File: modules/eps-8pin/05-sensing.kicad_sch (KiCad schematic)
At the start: 16 parts, among them U10 INA238, U11 INA238, U20 INA181A2IDBVR, U21 INA181A2IDBVR, U30 TLV7011DBVR, U31 TLV7011DBVR

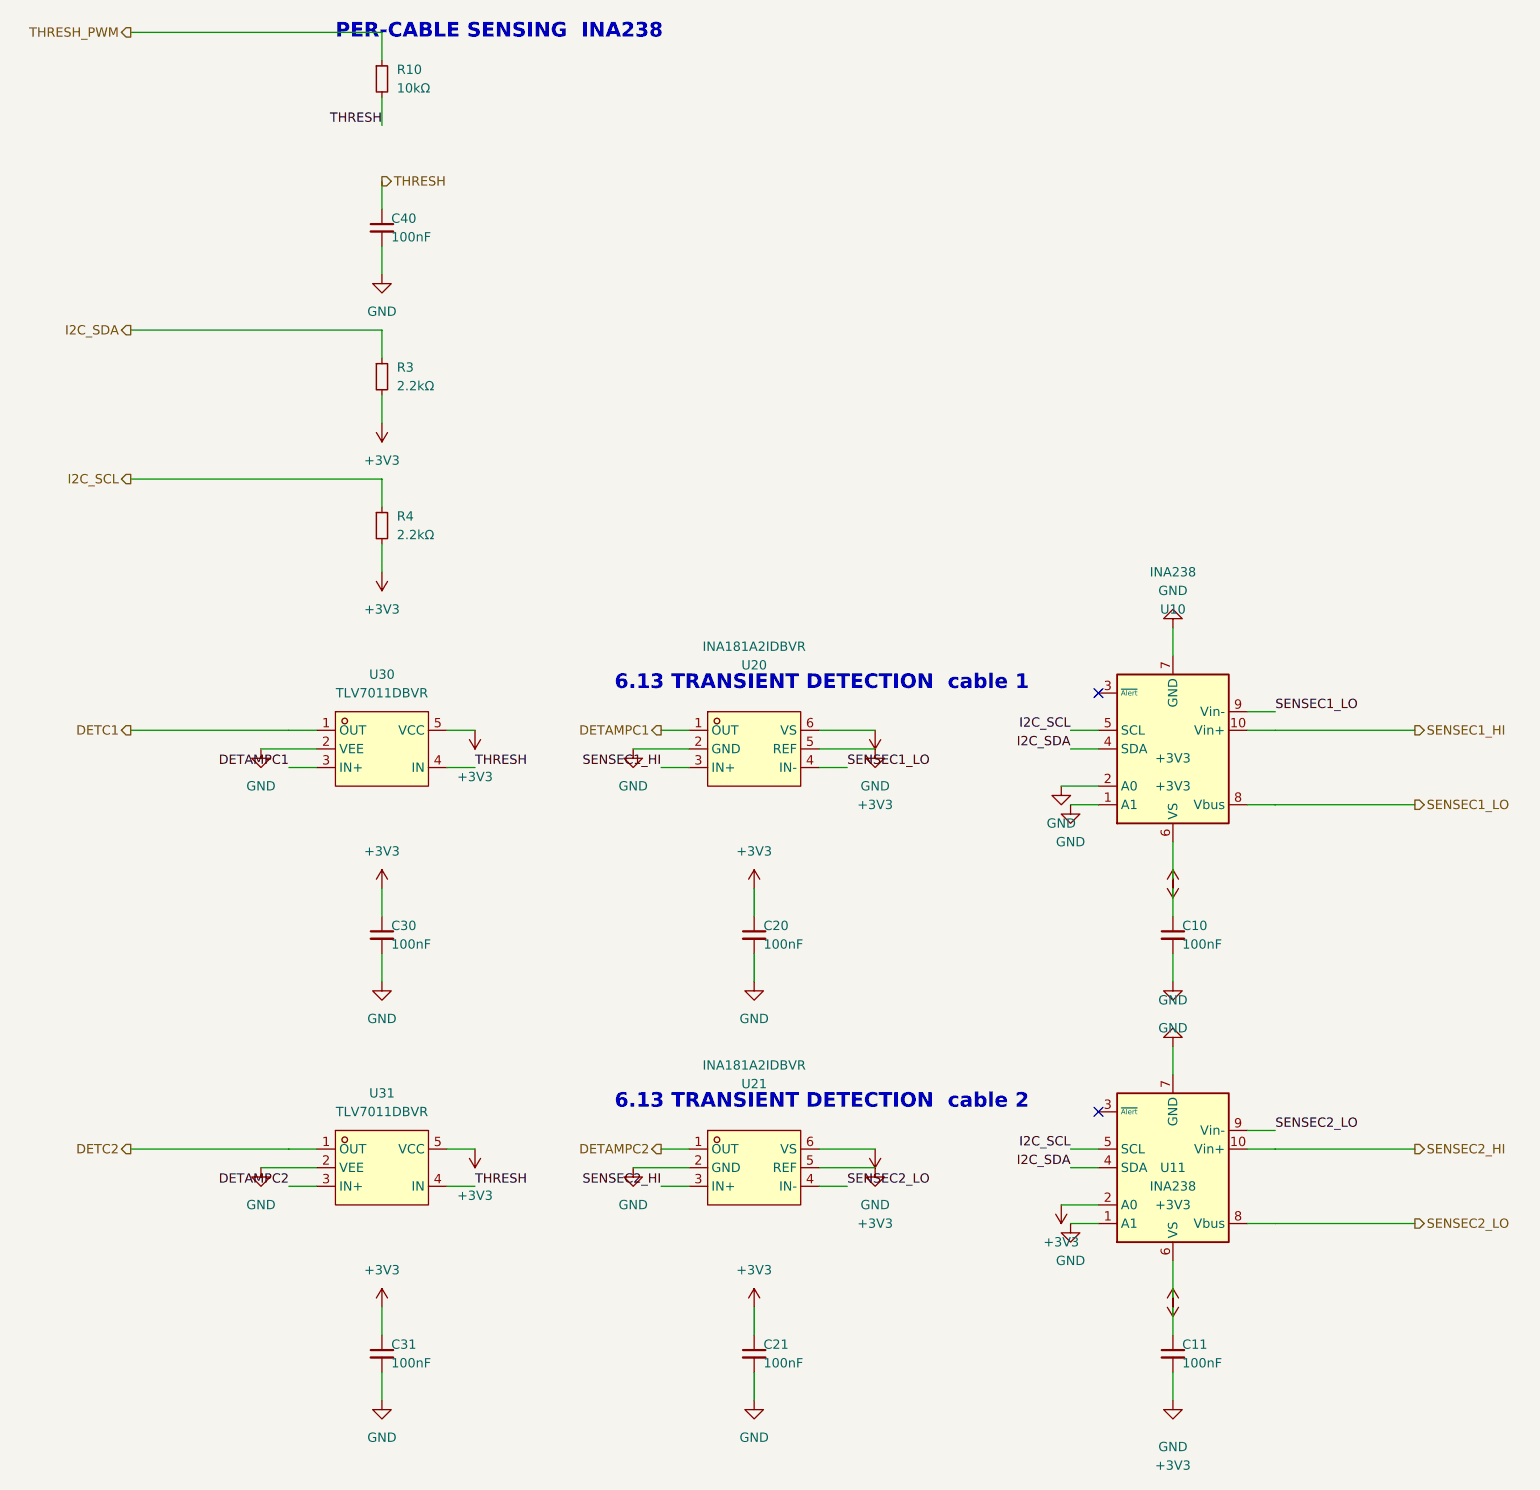
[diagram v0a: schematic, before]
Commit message: Looking through boards and figuring out outlines.
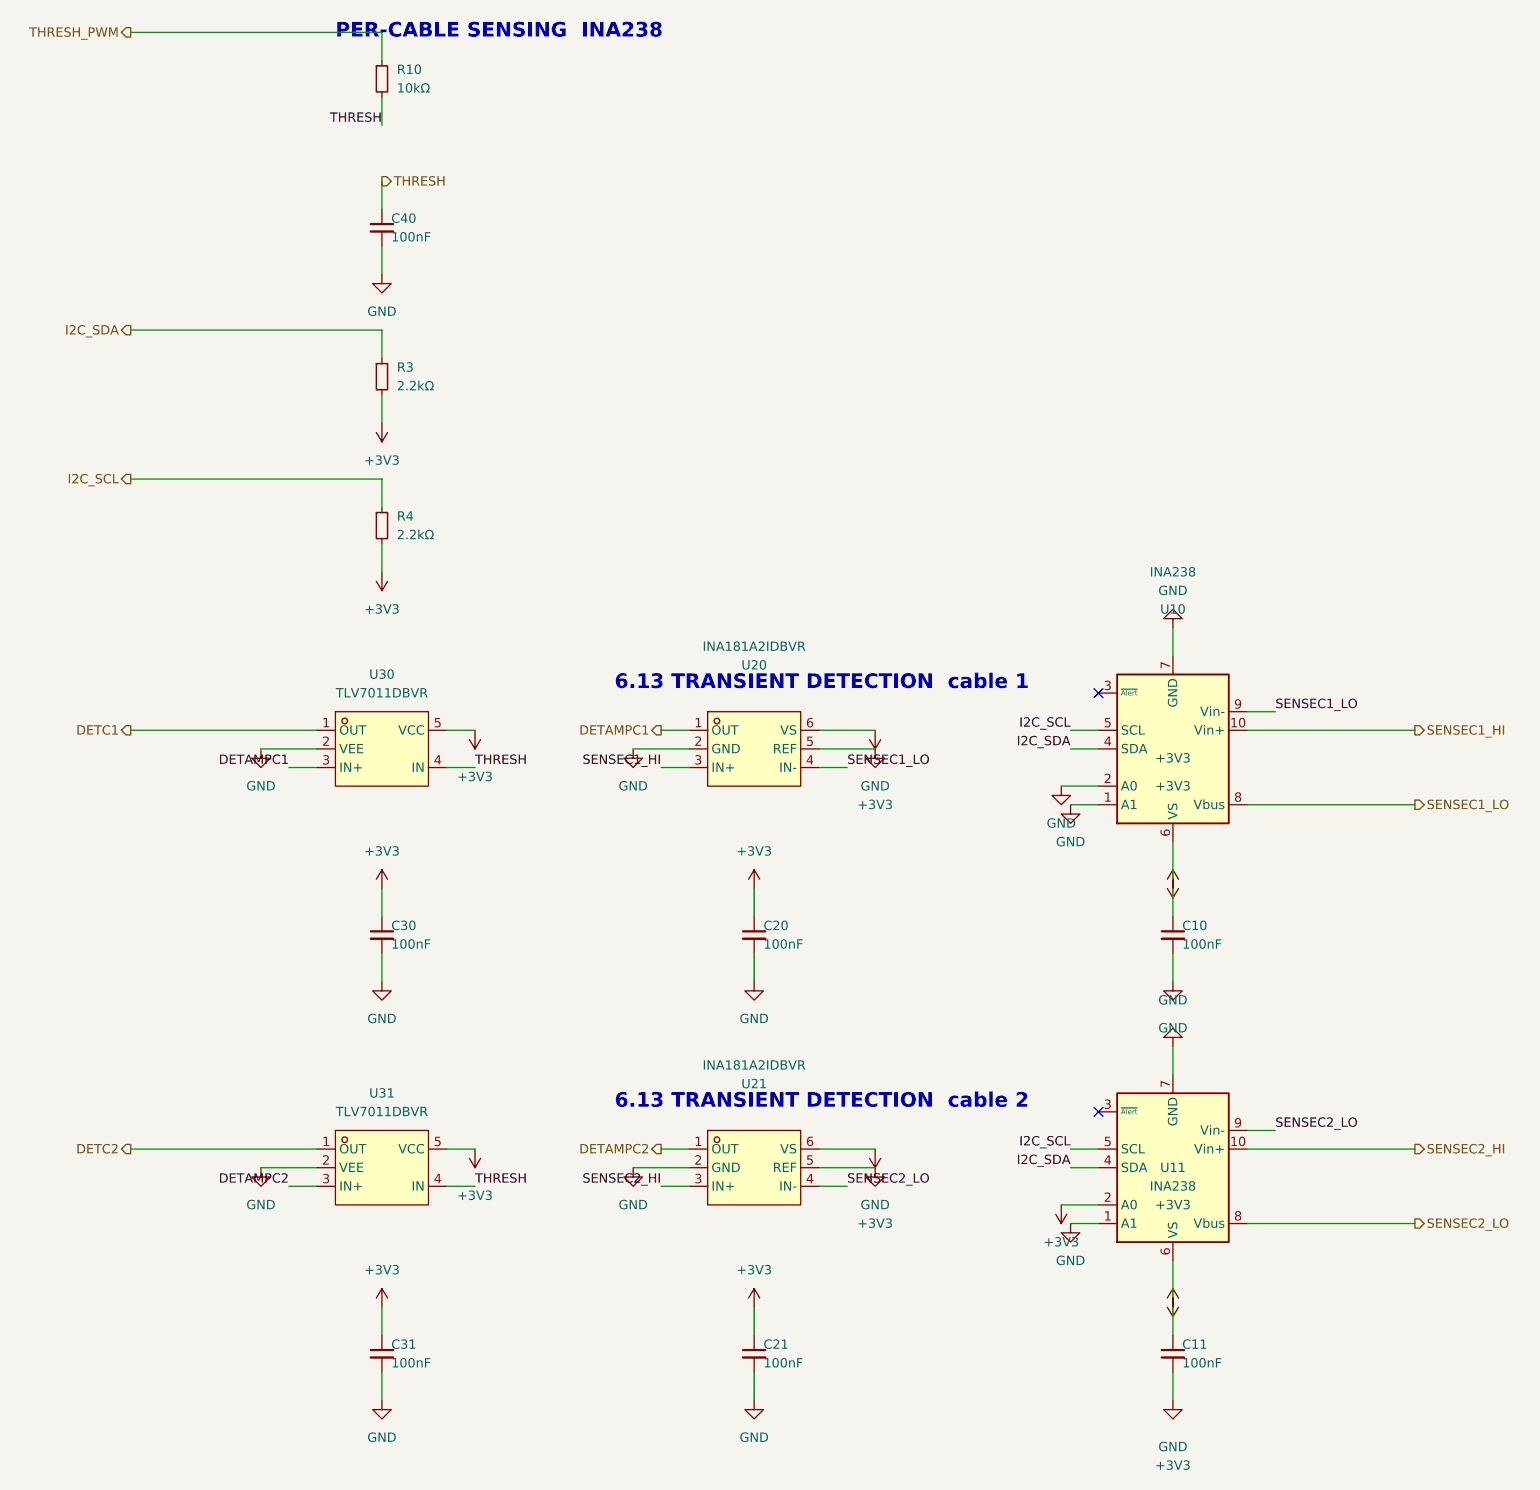
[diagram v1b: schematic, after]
